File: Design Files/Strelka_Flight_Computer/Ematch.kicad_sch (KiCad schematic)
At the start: 17 parts, among them Q10 AP2300, Q11 MMBT2222, Q8 AO3401A, Q9 AO3401A, U14 LM334M, U15 LM321

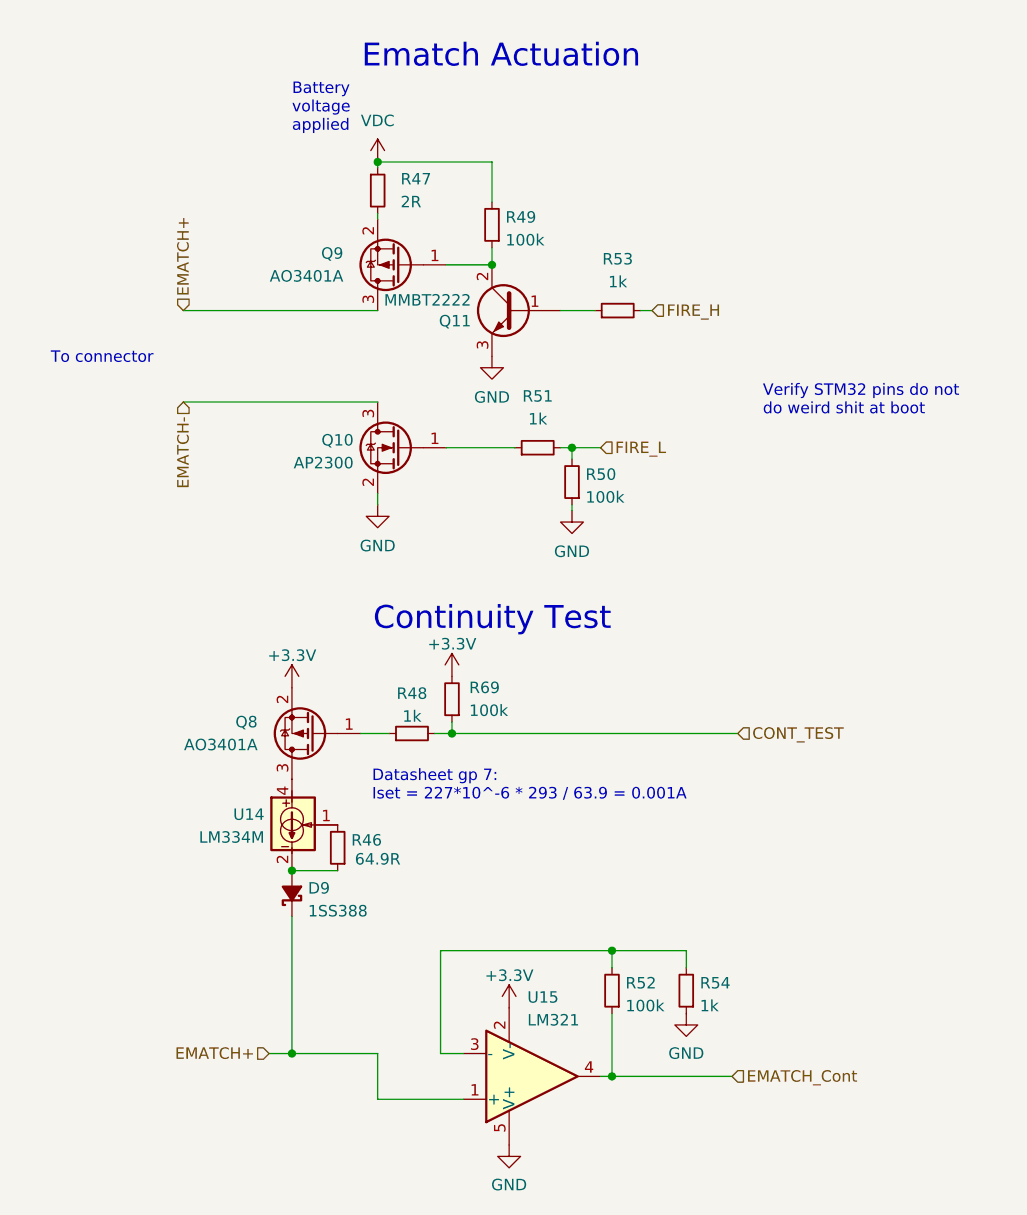
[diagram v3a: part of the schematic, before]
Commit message: Started component placement
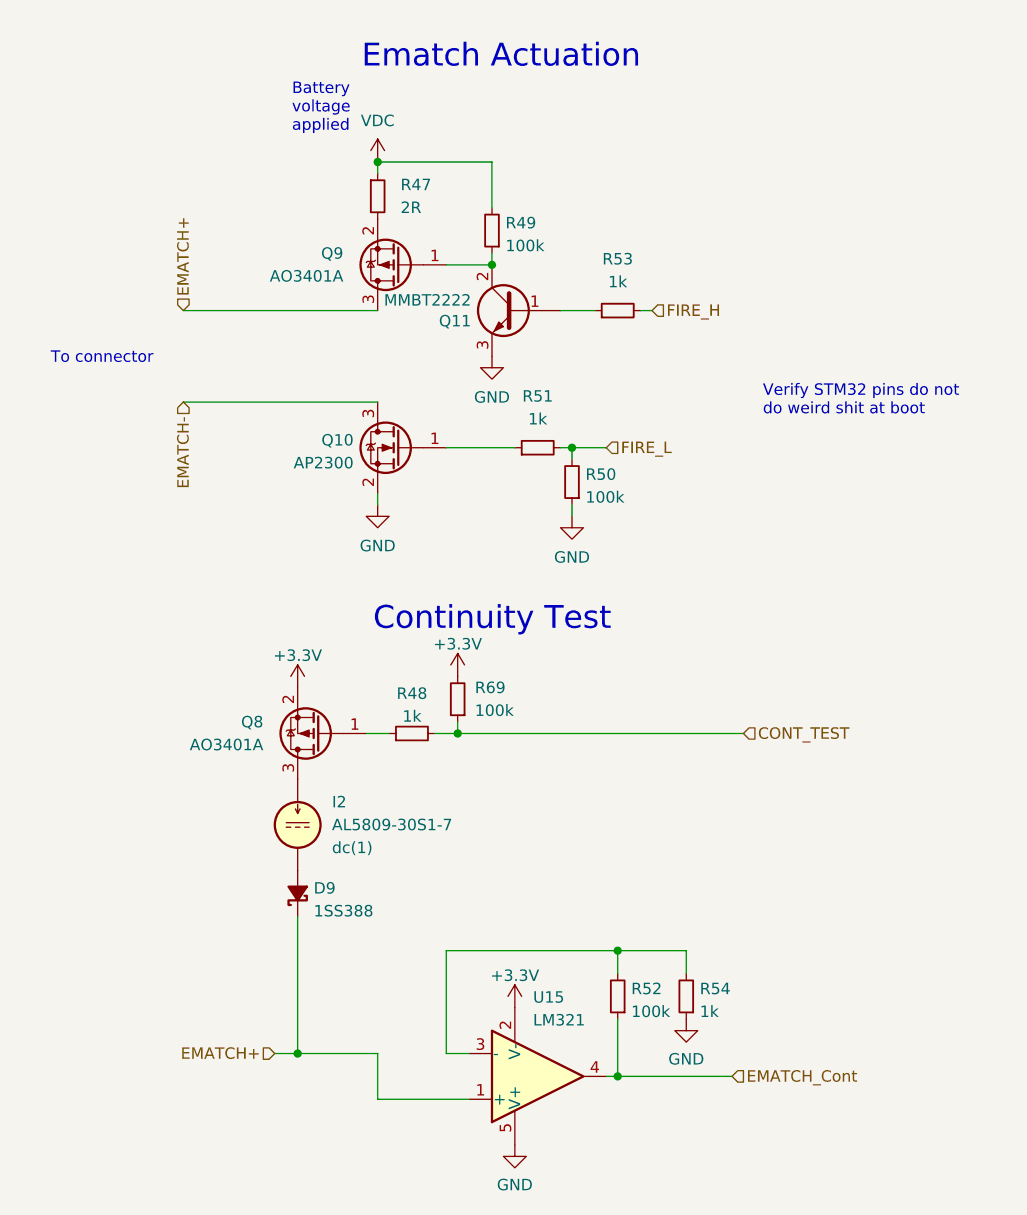
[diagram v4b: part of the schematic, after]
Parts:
- removed R46: 64.9R, Resistor_SMD:R_0603_1608Metric, symbol Device:R_Small
- removed U14: LM334M, Package_SO:SOIC-8_3.9x4.9mm_P1.27mm, symbol Reference_Current:LM334M
- added I2: AL5809-30S1-7, Diode_SMD:D_SOD-123, symbol Simulation_SPICE:IDC
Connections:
- net at Q8.3 (D): now also I2.1
- net at D9.2 (A): now also I2.2
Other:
- note removed: "Datasheet gp 7: Iset = 227*10^-6 * 293 / 63.9 = 0.001A"
- moved on the sheet: D9, Q8, R47, R49, R52, R54, R69, U15

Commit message: Creating BOM
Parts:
- I2: LCSC# (none) -> C151325; Spice_Model dc(1) -> (none); Spice_Netlist_Enabled Y -> (none); Spice_Primitive I -> (none)
- Q10: LCSC# (none) -> C360338
- Q11: LCSC# (none) -> C8512
- Q8, Q9: LCSC# (none) -> C347476
- U15: LCSC# (none) -> C5189111
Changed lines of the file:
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@@
     (effects (font (size 1.27 1.27)) (justify left))
   )
-  (symbol (lib_id "Device:R_Small") (at 161.29 135.89 180)
+  (symbol (lib_id "Device:R_Small") (at 161.29 135.89 180) (unit 1)
     (in_bom yes) (on_board yes) (fields_autoplaced)
     (property "Reference" "R54" (id 0) (at 162.7886 135.0553 0)
@@
     (pin "2")
   )
-  (symbol (lib_id "power:GND") (at 148.59 82.55 0)
+  (symbol (lib_id "power:GND") (at 148.59 82.55 0) (unit 1)
     (in_bom yes) (on_board yes)
     (property "Reference" "#PWR0192" (id 0) (at 148.59 88.9 0)
@@
     (pin "1")
   )
-  (symbol (lib_id "Device:R_Small") (at 135.89 102.87 180)
+  (symbol (lib_id "Device:R_Small") (at 135.89 102.87 180) (unit 1)
     (in_bom yes) (on_board yes) (fields_autoplaced)
     (property "Reference" "R69" (id 0) (at 137.795 101.5999 0)
@@
     (pin "2")
   )
-  (symbol (lib_id "power:GND") (at 161.29 138.43 0)
+  (symbol (lib_id "power:GND") (at 161.29 138.43 0) (unit 1)
     (in_bom yes) (on_board yes)
     (property "Reference" "#PWR0203" (id 0) (at 161.29 144.78 0)
@@
     (pin "1")
   )
-  (symbol (lib_id "Transistor_FET:AO3401A") (at 120.65 106.68 180)
+  (symbol (lib_id "Transistor_FET:AO3401A") (at 120.65 106.68 180) (unit 1)
     (in_bom yes) (on_board yes) (fields_autoplaced)
     (property "Reference" "Q8" (id 0) (at 114.3 105.4099 0)
@@
       (effects (font (size 1.27 1.27)) (justify left) hide)
     )
+    (property "LCSC#" "C347476" (id 4) (at 120.65 106.68 0)
+      (effects (font (size 1.27 1.27)) hide)
+    )
     (pin "1")
     (pin "2")
     (pin "3")
   )
-  (symbol (lib_id "Transistor_FET:2N7002E") (at 129.54 74.93 0) (mirror y)
+  (symbol (lib_id "Transistor_FET:2N7002E") (at 129.54 74.93 0) (mirror y) (unit 1)
     (in_bom yes) (on_board yes) (fields_autoplaced)
     (property "Reference" "Q10" (id 0) (at 124.3331 74.0953 0)
@@
       (effects (font (size 1.27 1.27)) (justify left) hide)
     )
+    (property "LCSC#" "C360338" (id 4) (at 129.54 74.93 0)
+      (effects (font (size 1.27 1.27)) hide)
+    )
     (pin "1")
     (pin "2")
     (pin "3")
   )
-  (symbol (lib_id "power:GND") (at 142.24 152.4 0)
+  (symbol (lib_id "power:GND") (at 142.24 152.4 0) (unit 1)
     (in_bom yes) (on_board yes)
     (property "Reference" "#PWR0194" (id 0) (at 142.24 158.75 0)
@@
     (pin "1")
   )
-  (symbol (lib_id "power:VDC") (at 127 43.18 0)
+  (symbol (lib_id "power:VDC") (at 127 43.18 0) (unit 1)
     (in_bom yes) (on_board yes) (fields_autoplaced)
     (property "Reference" "#PWR0191" (id 0) (at 127 45.72 0)
@@
     (pin "1")
   )
-  (symbol (lib_id "Amplifier_Operational:LM321") (at 144.78 144.78 0) (mirror x)
+  (symbol (lib_id "Amplifier_Operational:LM321") (at 144.78 144.78 0) (mirror x) (unit 1)
     (in_bom yes) (on_board yes) (fields_autoplaced)
     (property "Reference" "U15" (id 0) (at 144.2594 136.0002 0)
@@
     )
     (property "Datasheet" "http://www.ti.com/lit/ds/symlink/lm321.pdf" (id 3) (at 144.78 144.78 0)
+      (effects (font (size 1.27 1.27)) hide)
+    )
+    (property "LCSC#" "C5189111" (id 4) (at 144.78 144.78 0)
       (effects (font (size 1.27 1.27)) hide)
     )
@@
     (pin "5")
   )
-  (symbol (lib_id "Device:R_Small") (at 144.78 74.93 90)
+  (symbol (lib_id "Device:R_Small") (at 144.78 74.93 90) (unit 1)
     (in_bom yes) (on_board yes) (fields_autoplaced)
     (property "Reference" "R51" (id 0) (at 144.78 69.215 90))
@@
     (pin "2")
   )
-  (symbol (lib_id "Device:R_Small") (at 153.67 135.89 180)
+  (symbol (lib_id "Device:R_Small") (at 153.67 135.89 180) (unit 1)
     (in_bom yes) (on_board yes) (fields_autoplaced)
     (property "Reference" "R52" (id 0) (at 155.1686 135.0553 0)
@@
     (pin "2")
   )
-  (symbol (lib_id "power:+3.3V") (at 142.24 137.16 0)
+  (symbol (lib_id "power:+3.3V") (at 142.24 137.16 0) (unit 1)
     (in_bom yes) (on_board yes) (fields_autoplaced)
     (property "Reference" "#PWR0202" (id 0) (at 142.24 140.97 0)
@@
     (pin "1")
   )
-  (symbol (lib_id "Transistor_FET:AO3401A") (at 129.54 54.61 180)
+  (symbol (lib_id "Transistor_FET:AO3401A") (at 129.54 54.61 180) (unit 1)
     (in_bom yes) (on_board yes) (fields_autoplaced)
     (property "Reference" "Q9" (id 0) (at 123.19 53.3399 0)
@@
       (effects (font (size 1.27 1.27)) (justify left) hide)
     )
+    (property "LCSC#" "C347476" (id 4) (at 129.54 54.61 0)
+      (effects (font (size 1.27 1.27)) hide)
+    )
     (pin "1")
     (pin "2")
     (pin "3")
   )
-  (symbol (lib_id "Device:R_Small") (at 139.7 50.8 180)
+  (symbol (lib_id "Device:R_Small") (at 139.7 50.8 180) (unit 1)
     (in_bom yes) (on_board yes) (fields_autoplaced)
     (property "Reference" "R49" (id 0) (at 141.1986 49.9653 0)
@@
     (pin "2")
   )
-  (symbol (lib_id "Device:R_Small") (at 153.67 59.69 90)
+  (symbol (lib_id "Device:R_Small") (at 153.67 59.69 90) (unit 1)
     (in_bom yes) (on_board yes) (fields_autoplaced)
     (property "Reference" "R53" (id 0) (at 153.67 53.975 90))
@@
     (pin "2")
   )
-  (symbol (lib_id "Device:R_Small") (at 148.59 78.74 180)
+  (symbol (lib_id "Device:R_Small") (at 148.59 78.74 180) (unit 1)
     (in_bom yes) (on_board yes) (fields_autoplaced)
     (property "Reference" "R50" (id 0) (at 150.0886 77.9053 0)
@@
     (pin "2")
   )
-  (symbol (lib_id "power:GND") (at 127 81.28 0)
+  (symbol (lib_id "power:GND") (at 127 81.28 0) (unit 1)
     (in_bom yes) (on_board yes)
     (property "Reference" "#PWR0190" (id 0) (at 127 87.63 0)
@@
     (pin "1")
   )
-  (symbol (lib_id "power:GND") (at 139.7 64.77 0)
+  (symbol (lib_id "power:GND") (at 139.7 64.77 0) (unit 1)
     (in_bom yes) (on_board yes)
     (property "Reference" "#PWR0189" (id 0) (at 139.7 71.12 0)
@@
     (pin "1")
   )
-  (symbol (lib_id "Device:D_Schottky_Small_Filled") (at 118.11 124.46 90)
+  (symbol (lib_id "Device:D_Schottky_Small_Filled") (at 118.11 124.46 90) (unit 1)
     (in_bom yes) (on_board yes) (fields_autoplaced)
     (property "Reference" "D9" (id 0) (at 119.888 123.8793 90)
@@
     (pin "2")
   )
-  (symbol (lib_id "Device:R_Small") (at 130.81 106.68 90)
+  (symbol (lib_id "Device:R_Small") (at 130.81 106.68 90) (unit 1)
     (in_bom yes) (on_board yes) (fields_autoplaced)
     (property "Reference" "R48" (id 0) (at 130.81 102.2436 90))
@@
     (pin "2")
   )
-  (symbol (lib_id "Simulation_SPICE:IDC") (at 118.11 116.84 0)
+  (symbol (lib_id "Simulation_SPICE:IDC") (at 118.11 116.84 0) (unit 1)
     (in_bom yes) (on_board yes) (fields_autoplaced)
     (property "Reference" "I2" (id 0) (at 121.92 114.2999 0)
@@
       (effects (font (size 1.27 1.27)) hide)
     )
-    (property "Spice_Netlist_Enabled" "Y" (id 4) (at 118.11 116.84 0)
-      (effects (font (size 1.27 1.27)) (justify left) hide)
-    )
-    (property "Spice_Primitive" "I" (id 5) (at 118.11 116.84 0)
-      (effects (font (size 1.27 1.27)) (justify left) hide)
-    )
-    (property "Spice_Model" "dc(1)" (id 6) (at 121.92 119.3799 0)
-      (effects (font (size 1.27 1.27)) (justify left))
-    )
-    (pin "1")
-    (pin "2")
-  )
-  (symbol (lib_id "Device:Q_NPN_BCE") (at 142.24 59.69 0) (mirror y)
+    (property "LCSC#" "C151325" (id 4) (at 118.11 116.84 0)
+      (effects (font (size 1.27 1.27)) hide)
+    )
+    (pin "1")
+    (pin "2")
+  )
+  (symbol (lib_id "Device:Q_NPN_BCE") (at 142.24 59.69 0) (mirror y) (unit 1)
     (in_bom yes) (on_board yes)
     (property "Reference" "Q11" (id 0) (at 137.3886 60.8584 0)
@@
       (effects (font (size 1.27 1.27)) hide)
     )
+    (property "LCSC#" "C8512" (id 4) (at 142.24 59.69 0)
+      (effects (font (size 1.27 1.27)) hide)
+    )
     (pin "1")
     (pin "2")
     (pin "3")
   )
-  (symbol (lib_id "power:+3.3V") (at 135.89 100.33 0)
+  (symbol (lib_id "power:+3.3V") (at 135.89 100.33 0) (unit 1)
     (in_bom yes) (on_board yes) (fields_autoplaced)
     (property "Reference" "#PWR0226" (id 0) (at 135.89 104.14 0)
@@
     (pin "1")
   )
-  (symbol (lib_id "power:+3.3V") (at 118.11 101.6 0)
+  (symbol (lib_id "power:+3.3V") (at 118.11 101.6 0) (unit 1)
     (in_bom yes) (on_board yes) (fields_autoplaced)
     (property "Reference" "#PWR0193" (id 0) (at 118.11 105.41 0)
@@
     (pin "1")
   )
-  (symbol (lib_id "Device:R_Small") (at 127 46.99 0)
+  (symbol (lib_id "Device:R_Small") (at 127 46.99 0) (unit 1)
     (in_bom yes) (on_board yes) (fields_autoplaced)
     (property "Reference" "R47" (id 0) (at 129.54 45.7199 0)

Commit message: redo placement
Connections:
- net FIRE_L: now also R51.1; no longer R51.2
- net at Q10.1 (G): now also R51.2; no longer R51.1
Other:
- moved on the sheet: R50, R51, R52
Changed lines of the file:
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@@
   (junction (at 153.67 144.78) (diameter 0) (color 0 0 0 0)
+  )
+  (bus_entry (at 527.05 104.775) (size 2.54 2.54)
+    (stroke (width 0) (type default) (color 0 0 0 0))
   )
   (wire (pts (xy 153.67 144.78) (xy 166.37 144.78))
@@
     (effects (font (size 1.27 1.27)) (justify left))
   )
-  (symbol (lib_id "Device:R_Small") (at 161.29 135.89 180) (unit 1)
+  (symbol (lib_id "Device:R_Small") (at 161.29 135.89 180)
     (in_bom yes) (on_board yes) (fields_autoplaced)
     (property "Reference" "R54" (id 0) (at 162.7886 135.0553 0)
@@
     (pin "2")
   )
-  (symbol (lib_id "power:GND") (at 148.59 82.55 0) (unit 1)
+  (symbol (lib_id "power:GND") (at 148.59 82.55 0)
     (in_bom yes) (on_board yes)
     (property "Reference" "#PWR0192" (id 0) (at 148.59 88.9 0)
@@
     (pin "1")
   )
-  (symbol (lib_id "Device:R_Small") (at 135.89 102.87 180) (unit 1)
+  (symbol (lib_id "Device:R_Small") (at 135.89 102.87 180)
     (in_bom yes) (on_board yes) (fields_autoplaced)
     (property "Reference" "R69" (id 0) (at 137.795 101.5999 0)
@@
     (pin "2")
   )
-  (symbol (lib_id "power:GND") (at 161.29 138.43 0) (unit 1)
+  (symbol (lib_id "power:GND") (at 161.29 138.43 0)
     (in_bom yes) (on_board yes)
     (property "Reference" "#PWR0203" (id 0) (at 161.29 144.78 0)
@@
     (pin "1")
   )
-  (symbol (lib_id "Transistor_FET:AO3401A") (at 120.65 106.68 180) (unit 1)
+  (symbol (lib_id "Transistor_FET:AO3401A") (at 120.65 106.68 180)
     (in_bom yes) (on_board yes) (fields_autoplaced)
     (property "Reference" "Q8" (id 0) (at 114.3 105.4099 0)
@@
     (pin "3")
   )
-  (symbol (lib_id "Transistor_FET:2N7002E") (at 129.54 74.93 0) (mirror y) (unit 1)
+  (symbol (lib_id "Transistor_FET:2N7002E") (at 129.54 74.93 0) (mirror y)
     (in_bom yes) (on_board yes) (fields_autoplaced)
     (property "Reference" "Q10" (id 0) (at 124.3331 74.0953 0)
@@
     (pin "3")
   )
-  (symbol (lib_id "power:GND") (at 142.24 152.4 0) (unit 1)
+  (symbol (lib_id "power:GND") (at 142.24 152.4 0)
     (in_bom yes) (on_board yes)
     (property "Reference" "#PWR0194" (id 0) (at 142.24 158.75 0)
@@
     (pin "1")
   )
-  (symbol (lib_id "power:VDC") (at 127 43.18 0) (unit 1)
+  (symbol (lib_id "power:VDC") (at 127 43.18 0)
     (in_bom yes) (on_board yes) (fields_autoplaced)
     (property "Reference" "#PWR0191" (id 0) (at 127 45.72 0)
@@
     (pin "1")
   )
-  (symbol (lib_id "Amplifier_Operational:LM321") (at 144.78 144.78 0) (mirror x) (unit 1)
+  (symbol (lib_id "Amplifier_Operational:LM321") (at 144.78 144.78 0) (mirror x)
     (in_bom yes) (on_board yes) (fields_autoplaced)
     (property "Reference" "U15" (id 0) (at 144.2594 136.0002 0)
@@
     (pin "5")
   )
-  (symbol (lib_id "Device:R_Small") (at 144.78 74.93 90) (unit 1)
-    (in_bom yes) (on_board yes) (fields_autoplaced)
-    (property "Reference" "R51" (id 0) (at 144.78 69.215 90))
-    (property "Value" "1k" (id 1) (at 144.78 71.755 90))
+  (symbol (lib_id "Device:R_Small") (at 144.78 74.93 270) (mirror x)
+    (in_bom yes) (on_board yes) (fields_autoplaced)
+    (property "Reference" "R51" (id 0) (at 144.78 68.58 90))
+    (property "Value" "1k" (id 1) (at 144.78 71.12 90))
     (property "Footprint" "Resistor_SMD:R_0603_1608Metric" (id 2) (at 144.78 74.93 0)
       (effects (font (size 1.27 1.27)) hide)
@@
     (pin "2")
   )
-  (symbol (lib_id "Device:R_Small") (at 153.67 135.89 180) (unit 1)
-    (in_bom yes) (on_board yes) (fields_autoplaced)
-    (property "Reference" "R52" (id 0) (at 155.1686 135.0553 0)
-      (effects (font (size 1.27 1.27)) (justify right))
-    )
-    (property "Value" "100k" (id 1) (at 155.1686 137.5922 0)
+  (symbol (lib_id "Device:R_Small") (at 153.67 135.89 0) (mirror x)
+    (in_bom yes) (on_board yes) (fields_autoplaced)
+    (property "Reference" "R52" (id 0) (at 151.13 134.6199 0)
+      (effects (font (size 1.27 1.27)) (justify right))
+    )
+    (property "Value" "100k" (id 1) (at 151.13 137.1599 0)
       (effects (font (size 1.27 1.27)) (justify right))
     )
@@
     (pin "2")
   )
-  (symbol (lib_id "power:+3.3V") (at 142.24 137.16 0) (unit 1)
+  (symbol (lib_id "power:+3.3V") (at 142.24 137.16 0)
     (in_bom yes) (on_board yes) (fields_autoplaced)
     (property "Reference" "#PWR0202" (id 0) (at 142.24 140.97 0)
@@
     (pin "1")
   )
-  (symbol (lib_id "Transistor_FET:AO3401A") (at 129.54 54.61 180) (unit 1)
+  (symbol (lib_id "Transistor_FET:AO3401A") (at 129.54 54.61 180)
     (in_bom yes) (on_board yes) (fields_autoplaced)
     (property "Reference" "Q9" (id 0) (at 123.19 53.3399 0)
@@
     (pin "3")
   )
-  (symbol (lib_id "Device:R_Small") (at 139.7 50.8 180) (unit 1)
+  (symbol (lib_id "Device:R_Small") (at 139.7 50.8 180)
     (in_bom yes) (on_board yes) (fields_autoplaced)
     (property "Reference" "R49" (id 0) (at 141.1986 49.9653 0)
@@
     (pin "2")
   )
-  (symbol (lib_id "Device:R_Small") (at 153.67 59.69 90) (unit 1)
+  (symbol (lib_id "Device:R_Small") (at 153.67 59.69 90)
     (in_bom yes) (on_board yes) (fields_autoplaced)
     (property "Reference" "R53" (id 0) (at 153.67 53.975 90))
@@
     (pin "2")
   )
-  (symbol (lib_id "Device:R_Small") (at 148.59 78.74 180) (unit 1)
-    (in_bom yes) (on_board yes) (fields_autoplaced)
-    (property "Reference" "R50" (id 0) (at 150.0886 77.9053 0)
-      (effects (font (size 1.27 1.27)) (justify right))
-    )
-    (property "Value" "100k" (id 1) (at 150.0886 80.4422 0)
+  (symbol (lib_id "Device:R_Small") (at 148.59 78.74 0) (mirror x)
+    (in_bom yes) (on_board yes) (fields_autoplaced)
+    (property "Reference" "R50" (id 0) (at 146.05 77.4699 0)
+      (effects (font (size 1.27 1.27)) (justify right))
+    )
+    (property "Value" "100k" (id 1) (at 146.05 80.0099 0)
       (effects (font (size 1.27 1.27)) (justify right))
     )
@@
     (pin "2")
   )
-  (symbol (lib_id "power:GND") (at 127 81.28 0) (unit 1)
+  (symbol (lib_id "power:GND") (at 127 81.28 0)
     (in_bom yes) (on_board yes)
     (property "Reference" "#PWR0190" (id 0) (at 127 87.63 0)
@@
     (pin "1")
   )
-  (symbol (lib_id "power:GND") (at 139.7 64.77 0) (unit 1)
+  (symbol (lib_id "power:GND") (at 139.7 64.77 0)
     (in_bom yes) (on_board yes)
     (property "Reference" "#PWR0189" (id 0) (at 139.7 71.12 0)
@@
     (pin "1")
   )
-  (symbol (lib_id "Device:D_Schottky_Small_Filled") (at 118.11 124.46 90) (unit 1)
+  (symbol (lib_id "Device:D_Schottky_Small_Filled") (at 118.11 124.46 90)
     (in_bom yes) (on_board yes) (fields_autoplaced)
     (property "Reference" "D9" (id 0) (at 119.888 123.8793 90)
@@
     (pin "2")
   )
-  (symbol (lib_id "Device:R_Small") (at 130.81 106.68 90) (unit 1)
+  (symbol (lib_id "Device:R_Small") (at 130.81 106.68 90)
     (in_bom yes) (on_board yes) (fields_autoplaced)
     (property "Reference" "R48" (id 0) (at 130.81 102.2436 90))
@@
     (pin "2")
   )
-  (symbol (lib_id "Simulation_SPICE:IDC") (at 118.11 116.84 0) (unit 1)
+  (symbol (lib_id "Simulation_SPICE:IDC") (at 118.11 116.84 0)
     (in_bom yes) (on_board yes) (fields_autoplaced)
     (property "Reference" "I2" (id 0) (at 121.92 114.2999 0)
@@
     (pin "2")
   )
-  (symbol (lib_id "Device:Q_NPN_BCE") (at 142.24 59.69 0) (mirror y) (unit 1)
+  (symbol (lib_id "Device:Q_NPN_BCE") (at 142.24 59.69 0) (mirror y)
     (in_bom yes) (on_board yes)
     (property "Reference" "Q11" (id 0) (at 137.3886 60.8584 0)
@@
     (pin "3")
   )
-  (symbol (lib_id "power:+3.3V") (at 135.89 100.33 0) (unit 1)
+  (symbol (lib_id "power:+3.3V") (at 135.89 100.33 0)
     (in_bom yes) (on_board yes) (fields_autoplaced)
     (property "Reference" "#PWR0226" (id 0) (at 135.89 104.14 0)
@@
     (pin "1")
   )
-  (symbol (lib_id "power:+3.3V") (at 118.11 101.6 0) (unit 1)
+  (symbol (lib_id "power:+3.3V") (at 118.11 101.6 0)
     (in_bom yes) (on_board yes) (fields_autoplaced)
     (property "Reference" "#PWR0193" (id 0) (at 118.11 105.41 0)
@@
     (pin "1")
   )
-  (symbol (lib_id "Device:R_Small") (at 127 46.99 0) (unit 1)
+  (symbol (lib_id "Device:R_Small") (at 127 46.99 0)
     (in_bom yes) (on_board yes) (fields_autoplaced)
     (property "Reference" "R47" (id 0) (at 129.54 45.7199 0)
